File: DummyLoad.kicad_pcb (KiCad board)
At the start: 2 copper layers, 7 parts, among them Q1 IRFP250N, Q2 IRFP250N, Q3 IRFP250N, U1 LM324

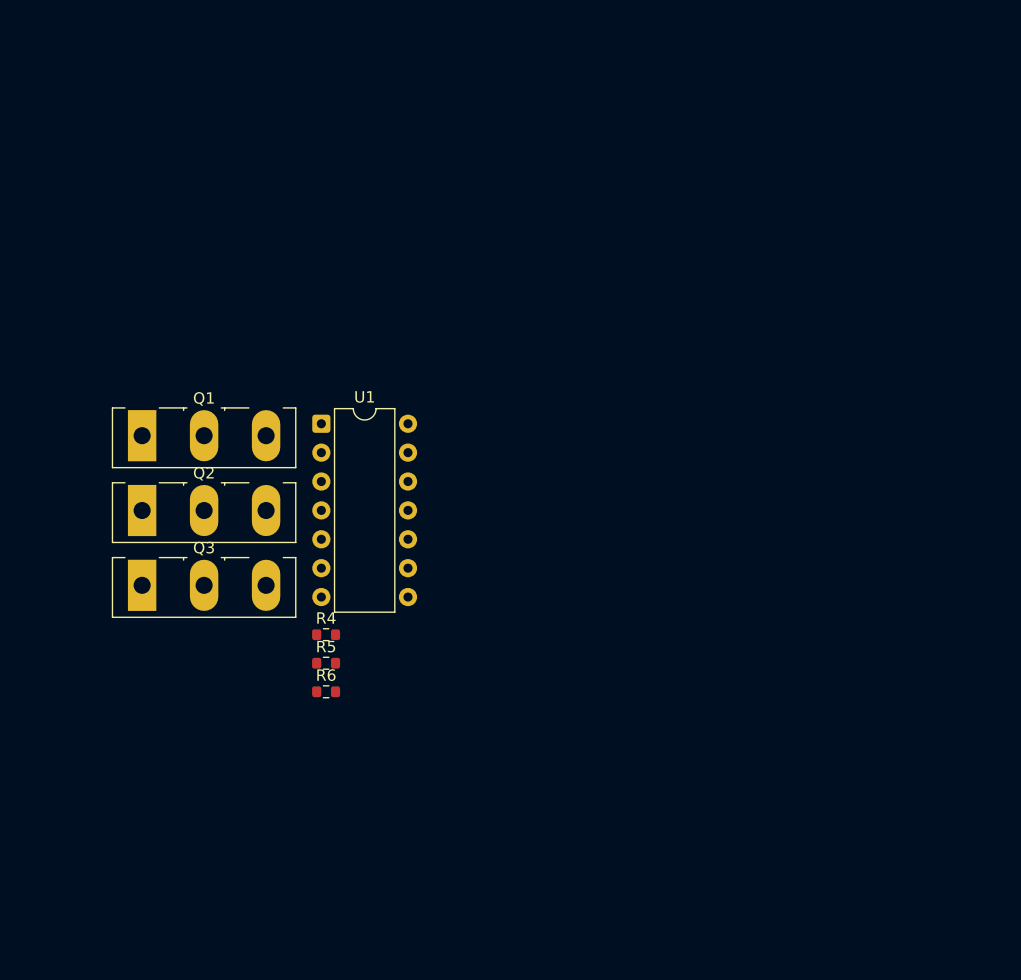
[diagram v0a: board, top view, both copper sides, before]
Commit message: Added README.md
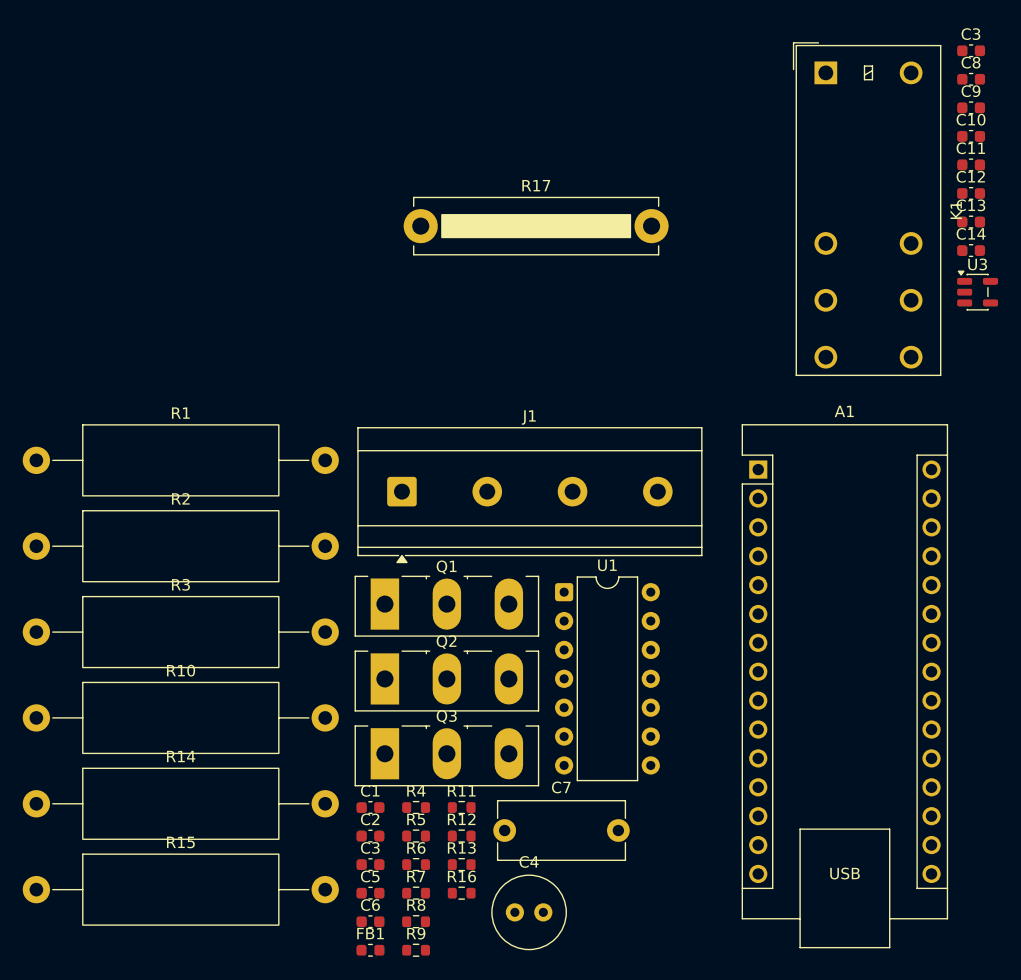
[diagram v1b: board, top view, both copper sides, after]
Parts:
- added A1: Arduino_Nano_Every, Module:Arduino_Nano, F.Cu at (189.5, 99.6)
- added C1: 100n, Capacitor_SMD:C_0603_1608Metric, F.Cu at (155.4, 129.3)
- added C10: 1n, Capacitor_SMD:C_0603_1608Metric, F.Cu at (208.2, 70.3)
- added C11: 10n, Capacitor_SMD:C_0603_1608Metric, F.Cu at (208.2, 72.8)
- added C12: 10n, Capacitor_SMD:C_0603_1608Metric, F.Cu at (208.2, 75.3)
- added C13: 10n, Capacitor_SMD:C_0603_1608Metric, F.Cu at (208.2, 77.8)
- added C14: 100n, Capacitor_SMD:C_0603_1608Metric, F.Cu at (208.2, 80.3)
- added C2: 2u2, Capacitor_SMD:C_0603_1608Metric, F.Cu at (155.4, 131.8)
- added C3: 100n, Capacitor_SMD:C_0603_1608Metric, F.Cu at (208.2, 62.8)
- added C3: 100n, Capacitor_SMD:C_0603_1608Metric, F.Cu at (155.4, 134.3)
- added C4: 100u, Capacitor_THT:C_Radial_D6.3mm_H7.0mm_P2.50mm, F.Cu at (168.1, 138.5)
- added C5: 100n, Capacitor_SMD:C_0603_1608Metric, F.Cu at (155.4, 136.8)
- added C6: 100n, Capacitor_SMD:C_0603_1608Metric, F.Cu at (155.4, 139.3)
- added C7: 100n, Capacitor_THT:C_Disc_D11.0mm_W5.0mm_P10.00mm, F.Cu at (167.2, 131.3)
- added C8: 1n, Capacitor_SMD:C_0603_1608Metric, F.Cu at (208.2, 65.3)
- added C9: 1n, Capacitor_SMD:C_0603_1608Metric, F.Cu at (208.2, 67.8)
- added FB1: 220R, Inductor_SMD:L_0603_1608Metric, F.Cu at (155.4, 141.9)
- added J1: YK3030423000G, TerminalBlock_MetzConnect:TerminalBlock_MetzConnect_Type175_RT02704HBLC_1x04_P7.50mm_Horizontal, F.Cu at (158.1, 101.5)
- added K1: G2RL-1-E, Relay_THT:Relay_SPDT_Omron_G2RL-1-E, F.Cu at (195.4, 64.7)
- added R1: 0R1, Resistor_THT:R_Axial_DIN0617_L17.0mm_D6.0mm_P25.40mm_Horizontal, F.Cu at (126.0, 98.8)
- added R10: 0R1, Resistor_THT:R_Axial_DIN0617_L17.0mm_D6.0mm_P25.40mm_Horizontal, F.Cu at (126.0, 121.4)
- added R11: 1k, Resistor_SMD:R_0603_1608Metric, F.Cu at (163.4, 129.3)
- added R12: 1k, Resistor_SMD:R_0603_1608Metric, F.Cu at (163.4, 131.8)
- added R13: 1k, Resistor_SMD:R_0603_1608Metric, F.Cu at (163.4, 134.3)
- added R14: 0R1, Resistor_THT:R_Axial_DIN0617_L17.0mm_D6.0mm_P25.40mm_Horizontal, F.Cu at (126.0, 129.0)
- added R15: 0R1, Resistor_THT:R_Axial_DIN0617_L17.0mm_D6.0mm_P25.40mm_Horizontal, F.Cu at (126.0, 136.5)
- added R16: 1M, Resistor_SMD:R_0603_1608Metric, F.Cu at (163.4, 136.8)
- added R17: 0R01, Resistor_THT:R_Bare_Metal_Element_L21.3mm_W4.8mm_P20.30mm, F.Cu at (159.8, 78.2)
- added R2: 0R1, Resistor_THT:R_Axial_DIN0617_L17.0mm_D6.0mm_P25.40mm_Horizontal, F.Cu at (126.0, 106.3)
- added R3: 0R1, Resistor_THT:R_Axial_DIN0617_L17.0mm_D6.0mm_P25.40mm_Horizontal, F.Cu at (126.0, 113.9)
- added R7: 220R, Resistor_SMD:R_0603_1608Metric, F.Cu at (159.4, 136.8)
- added R8: 220R, Resistor_SMD:R_0603_1608Metric, F.Cu at (159.4, 139.3)
- added R9: 220R, Resistor_SMD:R_0603_1608Metric, F.Cu at (159.4, 141.9)
- added U3: INA180A1, Package_TO_SOT_SMD:SOT-23-5, F.Cu at (208.7, 84.0)
- moved Q1 26.0 mm to (156.6, 111.4)
- moved Q2 26.0 mm to (156.6, 118.0)
- moved Q3 26.0 mm to (156.6, 124.6)
- moved U1 26.0 mm to (172.4, 110.4)
- moved R4 17.1 mm to (159.4, 129.3)
- moved R5 17.1 mm to (159.4, 131.8)
- moved R6 17.1 mm to (159.4, 134.3)
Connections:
- net Net-(Q1-D) renamed VIN
- U1 pad 1: unconnected-(U1-Pad1) -> Net-(C9-Pad2)
- U1 pad 10: unconnected-(U1C-+-Pad10) -> Net-(U1C-+)
- U1 pad 11: unconnected-(U1E-V--Pad11) -> Masa
- U1 pad 2: unconnected-(U1A---Pad2) -> /F0
- U1 pad 3: unconnected-(U1A-+-Pad3) -> Net-(U1A-+)
- U1 pad 4: unconnected-(U1E-V+-Pad4) -> +15V
- U1 pad 5: unconnected-(U1B-+-Pad5) -> Net-(U1B-+)
- U1 pad 6: unconnected-(U1B---Pad6) -> /F1
- U1 pad 7: unconnected-(U1-Pad7) -> Net-(C8-Pad2)
- U1 pad 8: unconnected-(U1-Pad8) -> Net-(C10-Pad2)
- U1 pad 9: unconnected-(U1C---Pad9) -> /F2

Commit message: sync
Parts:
- removed A1: Arduino_Nano_Every, Module:Arduino_Nano
- removed the C3 at (208.2, 62.8)
- removed the C3 at (155.4, 134.3)
- added C15: 100n, Capacitor_SMD:C_0603_1608Metric, F.Cu at (169.2, 150.5)
- added C16: 100n, Capacitor_SMD:C_0603_1608Metric, F.Cu at (89.1, 137.1)
- added C17: 100n, Capacitor_SMD:C_0603_1608Metric, F.Cu at (235.3, 108.4)
- added C18: 100n, Capacitor_SMD:C_0603_1608Metric, F.Cu at (223.5, 116.7)
- added C19: 2u2, Capacitor_SMD:C_0603_1608Metric, F.Cu at (225.2, 116.8)
- added C20: 100u, Capacitor_THT:C_Radial_D6.3mm_H7.0mm_P2.50mm, F.Cu at (229.2, 119.2)
- added C21: 100n, Capacitor_SMD:C_0603_1608Metric, F.Cu at (233.8, 119.7)
- added C22: 100n, Capacitor_SMD:C_0603_1608Metric, F.Cu at (65.7, 97.3)
- added C23: 100n, Capacitor_SMD:C_0603_1608Metric, F.Cu at (65.7, 99.8)
- added C24: 100n, Capacitor_SMD:C_0603_1608Metric, F.Cu at (65.7, 102.3)
- added C25: 100n, Capacitor_SMD:C_0603_1608Metric, F.Cu at (65.7, 104.8)
- added C26: 100n, Capacitor_SMD:C_0603_1608Metric, F.Cu at (89.1, 139.6)
- added C27: 2u2, Capacitor_SMD:C_0603_1608Metric, F.Cu at (89.1, 142.1)
- added C28: 100n, Capacitor_SMD:C_0603_1608Metric, F.Cu at (89.1, 144.6)
- added C29: 100n, Capacitor_SMD:C_0603_1608Metric, F.Cu at (93.7, 81.7)
- added C3: 100n, Capacitor_SMD:C_0603_1608Metric, F.Cu at (153.0, 96.8)
- added C30: 100n, Capacitor_SMD:C_0603_1608Metric, F.Cu at (93.7, 84.2)
- added C31: 100n, Capacitor_SMD:C_0603_1608Metric, F.Cu at (93.7, 86.7)
- added C32: 100n, Capacitor_SMD:C_0603_1608Metric, F.Cu at (93.7, 89.2)
- added C33: 100n, Capacitor_SMD:C_0603_1608Metric, F.Cu at (93.7, 91.7)
- added C34: 12p, Capacitor_SMD:C_0603_1608Metric, F.Cu at (93.7, 94.3)
- added C35: 12p, Capacitor_SMD:C_0603_1608Metric, F.Cu at (93.7, 96.8)
- added C36: 100n, Capacitor_SMD:C_0603_1608Metric, F.Cu at (97.7, 81.7)
- added C37: 100n, Capacitor_SMD:C_0603_1608Metric, F.Cu at (97.7, 84.2)
- added C39: 2u2, Capacitor_SMD:C_0603_1608Metric, F.Cu at (97.7, 86.7)
- added C40: 100n, Capacitor_SMD:C_0603_1608Metric, F.Cu at (97.7, 89.2)
- added C41: 100n, Capacitor_SMD:C_0603_1608Metric, F.Cu at (97.7, 91.7)
- added C42: 100n, Capacitor_SMD:C_0603_1608Metric, F.Cu at (97.7, 94.3)
- added C43: 100n, Capacitor_SMD:C_0603_1608Metric, F.Cu at (97.7, 96.8)
- added C44: 100n, Capacitor_SMD:C_0603_1608Metric, F.Cu at (89.1, 147.1)
- added C45: 22u, Capacitor_SMD:C_1206_3216Metric, F.Cu at (102.0, 140.8)
- added C46: 22u, Capacitor_SMD:C_1206_3216Metric, F.Cu at (102.0, 144.2)
- added C47: 100n, Capacitor_SMD:C_0603_1608Metric, F.Cu at (101.7, 81.7)
- added C48: 100n, Capacitor_SMD:C_0603_1608Metric, F.Cu at (101.7, 84.2)
- added C49: 22u, Capacitor_SMD:C_1206_3216Metric, F.Cu at (102.0, 147.5)
- added C50: 22u, Capacitor_SMD:C_1206_3216Metric, F.Cu at (102.0, 150.9)
- added C51: 22u, Capacitor_SMD:C_1206_3216Metric, F.Cu at (102.0, 154.2)
- added C52: 22u, Capacitor_SMD:C_1206_3216Metric, F.Cu at (107.6, 137.5)
- added C53: 100n, Capacitor_SMD:C_0603_1608Metric, F.Cu at (89.1, 149.6)
- added C54: 100n, Capacitor_SMD:C_0603_1608Metric, F.Cu at (89.1, 152.1)
- added C55: 22u, Capacitor_SMD:C_1206_3216Metric, F.Cu at (107.6, 140.8)
- added C56: 100n, Capacitor_SMD:C_0603_1608Metric, F.Cu at (93.1, 137.1)
- added C57: 22u, Capacitor_SMD:C_1206_3216Metric, F.Cu at (107.6, 144.2)
- added C58: 100n, Capacitor_SMD:C_0603_1608Metric, F.Cu at (93.1, 139.6)
- added C59: 100n, Capacitor_SMD:C_0603_1608Metric, F.Cu at (93.1, 142.1)
- added C60: 22u, Capacitor_SMD:C_1206_3216Metric, F.Cu at (107.6, 147.5)
- added C61: 22n, Capacitor_SMD:C_0603_1608Metric, F.Cu at (93.1, 144.6)
- added C62: 22u, Capacitor_SMD:C_1206_3216Metric, F.Cu at (107.6, 150.9)
- added C63: 100n, Capacitor_SMD:C_0603_1608Metric, F.Cu at (93.1, 147.1)
- added C64: 100n, Capacitor_SMD:C_0603_1608Metric, F.Cu at (93.1, 149.6)
- added D1: 1N4148W, Diode_SMD:D_SOD-123, F.Cu at (90.0, 155.0)
- added D2: 1N4148W, Diode_SMD:D_SOD-123, F.Cu at (170.2, 118.8)
- added FB2: 220R, Inductor_SMD:L_0603_1608Metric, F.Cu at (228.2, 115.8)
- added FB3: 120R, Inductor_SMD:L_0603_1608Metric, F.Cu at (101.7, 86.7)
- added J10: Screw_Terminal_01x03, Connector_PinHeader_2.54mm:PinHeader_1x03_P2.54mm_Vertical, F.Cu at (110.0, 82.7)
- added J11: Conn_01x04, Connector_PinHeader_2.54mm:PinHeader_1x04_P2.54mm_Vertical, F.Cu at (98.6, 100.3)
- added J12: USB4105-GF-A-120, Connector_USB:USB_C_Receptacle_G-Switch_GT-USB-7010ASV, F.Cu at (106.7, 103.4)
- added J13: Screw_Terminal_01x02, TerminalBlock:TerminalBlock_MaiXu_MX126-5.0-02P_1x02_P5.00mm, F.Cu at (95.2, 126.5)
- added J3: Conn_01x10, Connector_PinHeader_2.54mm:PinHeader_1x10_P2.54mm_Vertical, F.Cu at (237.5, 113.1)
- added J4: Conn_01x10, Connector_PinHeader_2.54mm:PinHeader_1x10_P2.54mm_Vertical, F.Cu at (39.7, 98.3)
- added J5: Conn_01x10, Connector_PinHeader_2.54mm:PinHeader_1x10_P2.54mm_Vertical, F.Cu at (44.3, 98.3)
- added J6: Conn_01x10, Connector_PinHeader_2.54mm:PinHeader_1x10_P2.54mm_Vertical, F.Cu at (48.9, 98.3)
- added J7: Conn_01x10, Connector_PinHeader_2.54mm:PinHeader_1x10_P2.54mm_Vertical, F.Cu at (53.5, 98.3)
- added J8: Conn_01x14, Connector_PinHeader_2.54mm:PinHeader_1x14_P2.54mm_Vertical, F.Cu at (77.3, 82.8)
- added J9: Conn_01x04, Connector_PinHeader_2.54mm:PinHeader_1x04_P2.54mm_Vertical, F.Cu at (94.0, 100.3)
- added L1: 15u, Inductor_SMD:L_APV_APH1240, F.Cu at (83.1, 128.6)
- added L2: 4u7, Inductor_SMD:L_APV_ANR5040, F.Cu at (107.1, 131.4)
- added M1: Fan_4pin, Connector:FanPinHeader_1x04_P2.54mm_Vertical, F.Cu at (81.8, 84.2)
- added M2: Fan_4pin, Connector:FanPinHeader_1x04_P2.54mm_Vertical, F.Cu at (81.8, 92.2)
- added M3: Fan_4pin, Connector:FanPinHeader_1x04_P2.54mm_Vertical, F.Cu at (81.8, 100.3)
- added M4: Fan_4pin, Connector:FanPinHeader_1x04_P2.54mm_Vertical, F.Cu at (81.8, 108.3)
- added Q4: 2N7002, Package_TO_SOT_SMD:SOT-23, F.Cu at (169.8, 122.5)
- added R18: 0R1, Resistor_THT:R_Bare_Metal_Element_L21.3mm_W4.8mm_P20.30mm, F.Cu at (179.9, 142.8)
- added R19: 4k7, Resistor_SMD:R_0603_1608Metric, F.Cu at (166.5, 122.4)
- added R20: 1k5, Resistor_SMD:R_0603_1608Metric, F.Cu at (101.7, 89.2)
- added R21: 4k7, Resistor_SMD:R_0603_1608Metric, F.Cu at (101.7, 91.7)
- added R22: 4k7, Resistor_SMD:R_0603_1608Metric, F.Cu at (101.7, 94.3)
- added R23: 10k, Resistor_SMD:R_0603_1608Metric, F.Cu at (101.7, 96.8)
- added R24: 10k, Resistor_SMD:R_0603_1608Metric, F.Cu at (105.7, 81.7)
- added R25: 0R, Resistor_SMD:R_0603_1608Metric, F.Cu at (105.7, 84.2)
- added R26: 10k, Resistor_SMD:R_0603_1608Metric, F.Cu at (65.7, 107.3)
- added R27: 100k, Resistor_SMD:R_0603_1608Metric, F.Cu at (69.7, 97.3)
- added R28: 100R, Resistor_SMD:R_0603_1608Metric, F.Cu at (105.7, 86.7)
- added R29: 10k, Resistor_SMD:R_0603_1608Metric, F.Cu at (69.7, 99.8)
- added R30: 10k, Resistor_SMD:R_0603_1608Metric, F.Cu at (69.7, 102.3)
- added R31: 10k, Resistor_SMD:R_0603_1608Metric, F.Cu at (69.7, 104.8)
- added R32: 10k, Resistor_SMD:R_0603_1608Metric, F.Cu at (69.7, 107.3)
- added R33: 5k1, Resistor_SMD:R_0603_1608Metric, F.Cu at (105.7, 89.2)
- added R34: 5k1, Resistor_SMD:R_0603_1608Metric, F.Cu at (105.7, 91.7)
- added R35: 5k1, Resistor_SMD:R_0603_1608Metric, F.Cu at (105.7, 94.3)
- added R36: 100k, Resistor_SMD:R_0603_1608Metric, F.Cu at (97.1, 137.1)
- added R37: 9k, Resistor_SMD:R_0603_1608Metric, F.Cu at (97.1, 139.6)
- added R38: 100k, Resistor_SMD:R_0603_1608Metric, F.Cu at (97.1, 142.1)
- added R39: 22k, Resistor_SMD:R_0603_1608Metric, F.Cu at (97.1, 144.6)
- added R40: 100k, Resistor_SMD:R_0603_1608Metric, F.Cu at (97.1, 147.1)
- added RV1: 10k, Potentiometer_THT:Potentiometer_ACP_CA14-H5_Horizontal, F.Cu at (39.3, 83.2)
- added RV2: 50k, Potentiometer_THT:Potentiometer_ACP_CA14-H4_Horizontal, F.Cu at (57.7, 98.8)
- added RV3: 10k, Potentiometer_THT:Potentiometer_ACP_CA14-H5_Horizontal, F.Cu at (48.2, 83.2)
- added RV4: 10k, Potentiometer_THT:Potentiometer_ACP_CA14-H5_Horizontal, F.Cu at (57.1, 83.2)
- added RV5: 10k, Potentiometer_THT:Potentiometer_ACP_CA14-H5_Horizontal, F.Cu at (66.0, 83.2)
- added U10: TMP102xxDRL, Package_TO_SOT_SMD:SOT-563, F.Cu at (109.5, 91.8)
- added U11: L7815, Package_TO_SOT_SMD:TO-252-2, F.Cu at (81.9, 140.0)
- added U12: MCP4728, Package_SO:MSOP-10_3x3mm_P0.5mm, F.Cu at (67.8, 118.5)
- added U13: L7805, Package_TO_SOT_SMD:TO-252-2, F.Cu at (81.9, 148.2)
- added U14: SD8942, Package_TO_SOT_SMD:SOT-23-6, F.Cu at (77.5, 154.6)
- added U2: ADS1115IDGS, Package_SO:TSSOP-10_3x3mm_P0.5mm, F.Cu at (67.9, 113.8)
- added U4: INA180A1, Package_TO_SOT_SMD:SOT-23-5, F.Cu at (169.2, 147.8)
- added U5: 74HC4051, Package_SO:SOIC-16_3.9x9.9mm_P1.27mm, F.Cu at (60.0, 117.5)
- added U6: LMR33630ADDA, Package_SO:Texas_HSOP-8-1EP_3.9x4.9mm_P1.27mm_ThermalVias, F.Cu at (108.0, 124.8)
- added U7: STM32G431C6Tx, Package_QFP:LQFP-48_7x7mm_P0.5mm, F.Cu at (106.6, 113.8)
- added U8: USBLC6-2SC6, Package_TO_SOT_SMD:SOT-23-6, F.Cu at (87.8, 115.0)
- added U9: FM24C64B, Package_SO:SOIC-8_3.9x4.9mm_P1.27mm, F.Cu at (95.9, 113.6)
- added Y1: Crystal_GND24, Crystal:Crystal_SMD_EuroQuartz_X22-4Pin_2.5x2.0mm_HandSoldering, F.Cu at (82.4, 115.1)
- C6: value 100n -> 22u; footprint Capacitor_SMD:C_0603_1608Metric -> Capacitor_SMD:C_1206_3216Metric
- R16: value 1M -> 100k
- moved R15 93.3 mm to (205.8, 88.0), turned to -90 degrees
- moved R3 90.8 mm to (213.0, 88.0), turned to -90 degrees
- moved C5 82.2 mm to (233.8, 112.2), turned to 90 degrees
- moved FB1 78.5 mm to (228.2, 112.5)
- moved R14 74.5 mm to (188.2, 88.0), turned to -90 degrees
- moved C10 73.6 mm to (146.5, 110.5), turned to 180 degrees
- moved C2 72.7 mm to (225.2, 111.8), turned to 90 degrees
- moved R16 71.9 mm to (93.1, 152.1)
- moved R2 71.9 mm to (195.5, 88.0), turned to -90 degrees
- moved C1 70.4 mm to (223.5, 111.8), turned to 90 degrees
- moved C8 69.0 mm to (147.0, 97.2), turned to 180 degrees
- moved C4 68.1 mm to (229.5, 109.2), turned to 90 degrees
- moved J1 68.0 mm to (201.2, 154.1), turned to 180 degrees
- moved K1 67.0 mm to (175.5, 128.7), turned to 90 degrees
- moved C13 66.0 mm to (151.2, 111.2)
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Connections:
- C6 pad 1: /Set -> +12V
- K1 pad 14: unconnected-(K1-Pad14) -> Net-(U4-+)
- K1 pad A1: unconnected-(K1-PadA1) -> Net-(D2-A)
- K1 pad A2: unconnected-(K1-PadA2) -> +24V
- R16 pad 1: Masa -> Net-(U6-PG)
- R16 pad 2: /Set -> Net-(U6-VCC)
- U3 pad 1: /Sense -> /Sense0
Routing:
- net VIN: track 0.00 -> 211.2 mm
- net /Set: track 0.00 -> 167.6 mm
- net Masa: track 0.00 -> 109.0 mm, vias 0 -> 7
- net /F2: track 0.00 -> 94.3 mm, vias 0 -> 2
- net +5V: track 0.00 -> 91.7 mm, vias 0 -> 2
- net +24V: track 0.00 -> 84.4 mm
- net /RangeSelect: track 0.00 -> 83.0 mm, vias 0 -> 4
- net +15V: track 0.00 -> 82.4 mm, vias 0 -> 2
- net /Sense0: track 0.00 -> 81.9 mm, vias 0 -> 2
- net /Sense1: track 0.00 -> 75.5 mm
- net /G2: track 0.00 -> 74.6 mm
- net /F1: track 0.00 -> 66.4 mm
- net Net-(K1-Pad11): track 0.00 -> 56.6 mm
- net /G1: track 0.00 -> 48.2 mm
- net Net-(U4-+): track 0.00 -> 45.3 mm
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- added copper zone on B.Cu, net Masa
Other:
- board outline added: 100 x 80 mm
- board text added: "GND"
- board text added: "VIN"

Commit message: sync
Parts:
- removed C16, C22, C23, C24, C25, C26, C28, C29, C30, C31, C32, C33, C36, C37, C40, C41, C42, C43, C44, C47, C48, C53, C54, C56, C58, C59, C63, C64: 100n, Capacitor_SMD:C_0603_1608Metric
- removed C27, C39: 2u2, Capacitor_SMD:C_0603_1608Metric
- removed C34, C35: 12p, Capacitor_SMD:C_0603_1608Metric
- removed C45, C46, C49, C50, C51, C52, C55, C57, C6, C60, C62: 22u, Capacitor_SMD:C_1206_3216Metric
- removed C61: 22n, Capacitor_SMD:C_0603_1608Metric
- removed D1: 1N4148W, Diode_SMD:D_SOD-123
- removed FB3: 120R, Inductor_SMD:L_0603_1608Metric
- removed J10: Screw_Terminal_01x03, Connector_PinHeader_2.54mm:PinHeader_1x03_P2.54mm_Vertical
- removed J11, J9: Conn_01x04, Connector_PinHeader_2.54mm:PinHeader_1x04_P2.54mm_Vertical
- removed J12: USB4105-GF-A-120, Connector_USB:USB_C_Receptacle_G-Switch_GT-USB-7010ASV
- removed J13: Screw_Terminal_01x02, TerminalBlock:TerminalBlock_MaiXu_MX126-5.0-02P_1x02_P5.00mm
- removed J4, J5, J6, J7: Conn_01x10, Connector_PinHeader_2.54mm:PinHeader_1x10_P2.54mm_Vertical
- removed J8: Conn_01x14, Connector_PinHeader_2.54mm:PinHeader_1x14_P2.54mm_Vertical
- removed L1: 15u, Inductor_SMD:L_APV_APH1240
- removed L2: 4u7, Inductor_SMD:L_APV_ANR5040
- removed M1, M2, M3, M4: Fan_4pin, Connector:FanPinHeader_1x04_P2.54mm_Vertical
- removed R16, R27, R36, R38, R40: 100k, Resistor_SMD:R_0603_1608Metric
- removed R20: 1k5, Resistor_SMD:R_0603_1608Metric
- removed R21, R22: 4k7, Resistor_SMD:R_0603_1608Metric
- removed R23, R24, R26, R29, R30, R31, R32: 10k, Resistor_SMD:R_0603_1608Metric
- removed R25: 0R, Resistor_SMD:R_0603_1608Metric
- removed R28: 100R, Resistor_SMD:R_0603_1608Metric
- removed R33, R34, R35: 5k1, Resistor_SMD:R_0603_1608Metric
- removed R37: 9k, Resistor_SMD:R_0603_1608Metric
- removed R39: 22k, Resistor_SMD:R_0603_1608Metric
- removed RV1, RV3, RV4, RV5: 10k, Potentiometer_THT:Potentiometer_ACP_CA14-H5_Horizontal
- removed RV2: 50k, Potentiometer_THT:Potentiometer_ACP_CA14-H4_Horizontal
- removed U10: TMP102xxDRL, Package_TO_SOT_SMD:SOT-563
- removed U11: L7815, Package_TO_SOT_SMD:TO-252-2
- removed U12: MCP4728, Package_SO:MSOP-10_3x3mm_P0.5mm
- removed U13: L7805, Package_TO_SOT_SMD:TO-252-2
- removed U14: SD8942, Package_TO_SOT_SMD:SOT-23-6
- removed U2: ADS1115IDGS, Package_SO:TSSOP-10_3x3mm_P0.5mm
- removed U5: 74HC4051, Package_SO:SOIC-16_3.9x9.9mm_P1.27mm
- removed U6: LMR33630ADDA, Package_SO:Texas_HSOP-8-1EP_3.9x4.9mm_P1.27mm_ThermalVias
- removed U7: STM32G431C6Tx, Package_QFP:LQFP-48_7x7mm_P0.5mm
- removed U8: USBLC6-2SC6, Package_TO_SOT_SMD:SOT-23-6
- removed U9: FM24C64B, Package_SO:SOIC-8_3.9x4.9mm_P1.27mm
- removed Y1: Crystal_GND24, Crystal:Crystal_SMD_EuroQuartz_X22-4Pin_2.5x2.0mm_HandSoldering
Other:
- board size 100 x 80 mm -> 100 x 81 mm
